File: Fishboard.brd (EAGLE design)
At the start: 47.9 x 61 mm, 23 parts, among them J3 B1, J4 B2, J5 B3, J7 B4, Q1 FQP30N06L, Q2 FQP30N06L, Q3 FQP30N06L

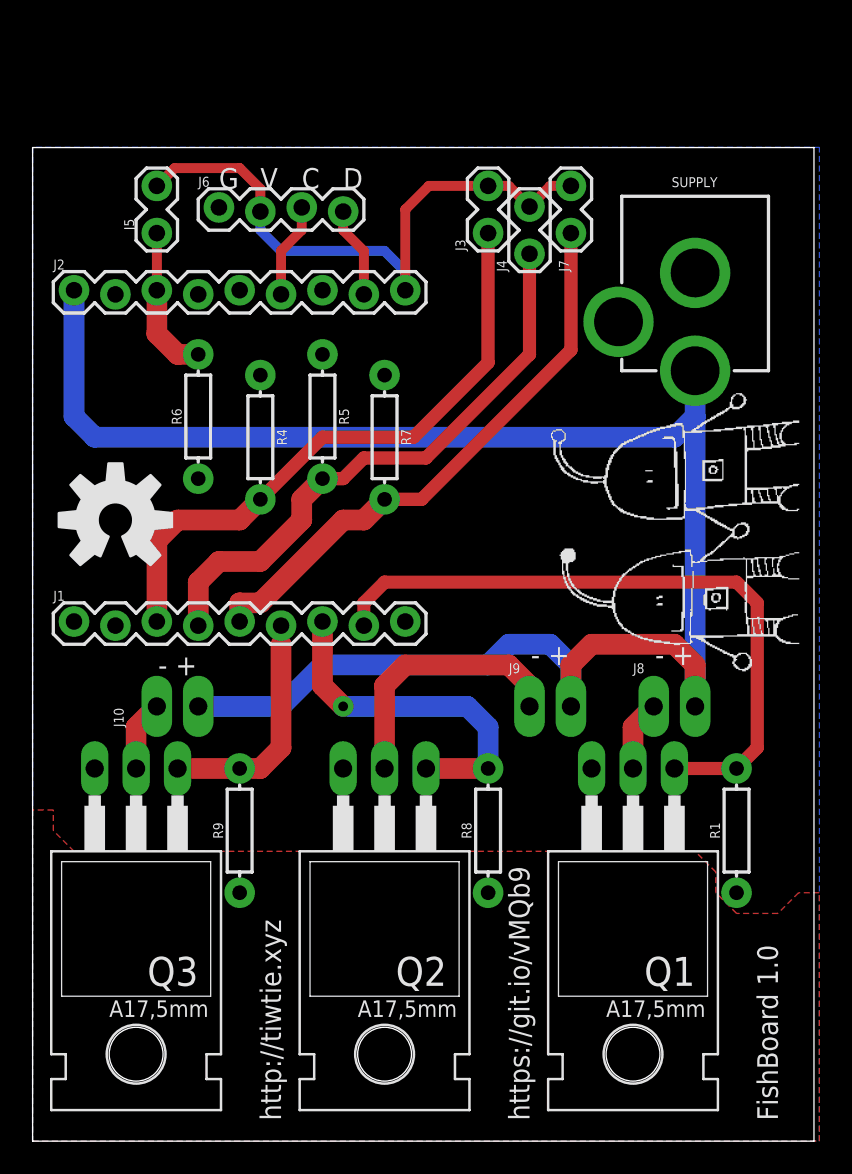
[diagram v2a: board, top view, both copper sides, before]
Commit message: Replaced TIP120 part with custom part so that we can correctly route it.
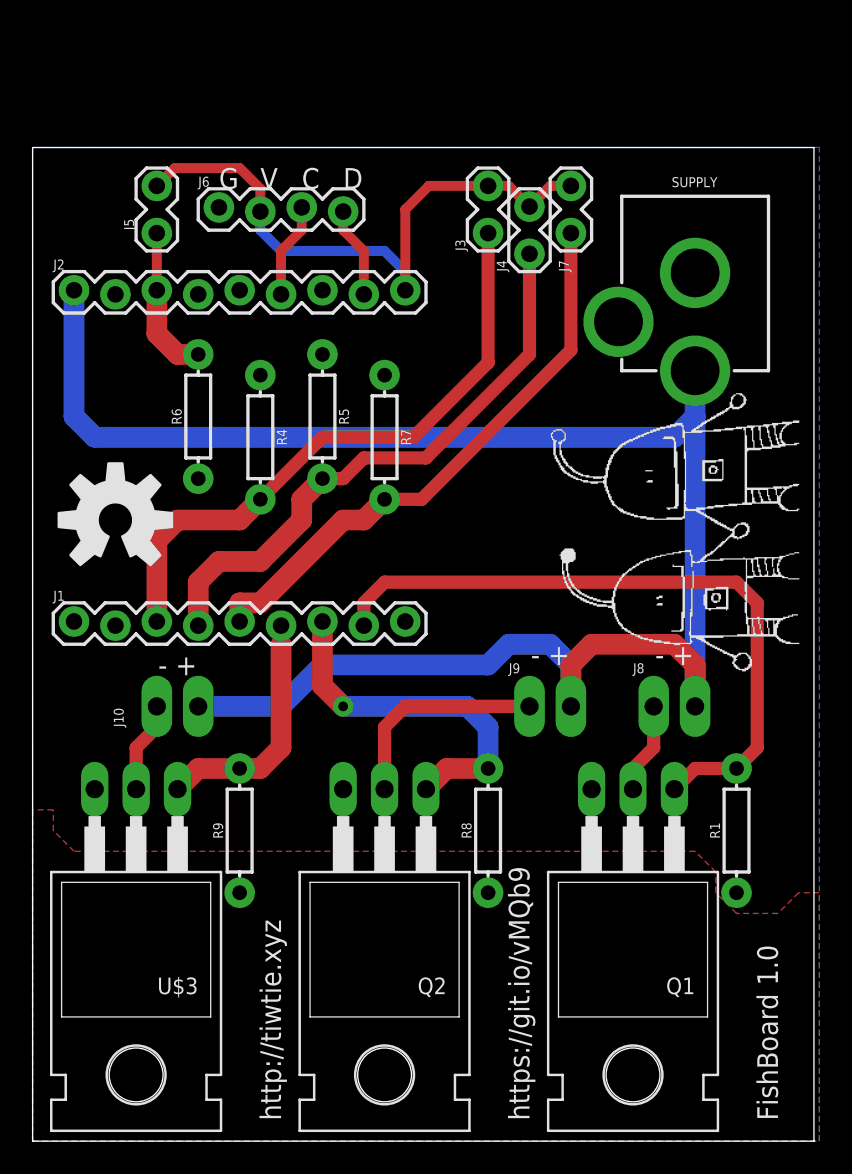
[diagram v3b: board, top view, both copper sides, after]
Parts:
- removed Q3: FQP30N06L, transistor-power:TO220AH
- added U$3: FQP30N06L, fishlib:TO220
- Q1, Q2: device transistor-power:TO220AH -> fishlib:TO220
- moved Q1 1.27 mm to (36.8, 15.2)
- moved Q2 1.27 mm to (21.6, 15.2)
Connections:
- removed net N$5: J9.1, Q2.C
- removed net N$6: J10.1, Q3.C
- new net N$2: J8.1, Q1.D
- new net N$4: J10.1, U$3.D
- net DEV1_EN: now also Q1.G; no longer Q1.B
- net DEV2_EN: now also Q2.G; no longer Q2.B
- net DEV3_EN: now also U$3.G; no longer Q3.B
- net GND: now also Q1.S, Q2.S, U$3.S; no longer Q1.E, Q2.E, Q3.E
- net N$1: now also J9.1, Q2.D; no longer J8.1, Q1.C
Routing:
- net N$5: track 16.3 -> 0.00 mm
- net N$1: track 4.34 -> 13.2 mm
- net N$2: track 0.00 -> 5.61 mm
- net N$4: track 0.00 -> 5.61 mm
- net N$6: track 4.34 -> 0.00 mm
- net DEV3_EN: track 14.4 -> 14.9 mm
- net DEV2_EN: track 21.5 -> 22.0 mm
- net DEV1_EN: track 41.1 -> 41.6 mm
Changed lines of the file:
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@@
 <element name="J1" library="SparkFun-Connectors" package="1X09_LOCK" value="" x="2.54" y="31.75"/>
 <element name="J2" library="SparkFun-Connectors" package="1X09_LOCK" value="" x="2.54" y="52.07"/>
-<element name="Q1" library="transistor-power" package="TO220AH" value="FQP30N06L" x="36.83" y="16.51" smashed="yes" rot="R180">
-<attribute name="NAME" x="40.64" y="11.303" size="1.778" layer="25" ratio="10" rot="R180"/>
-<attribute name="VALUE" x="40.767" y="13.97" size="1.016" layer="27" font="vector" ratio="10" rot="R180"/>
-</element>
-<element name="Q2" library="transistor-power" package="TO220AH" value="FQP30N06L" x="21.59" y="16.51" smashed="yes" rot="R180">
-<attribute name="NAME" x="25.4" y="11.303" size="1.778" layer="25" ratio="10" rot="R180"/>
-<attribute name="VALUE" x="25.527" y="13.97" size="1.016" layer="27" font="vector" ratio="10" rot="R180"/>
-</element>
-<element name="Q3" library="transistor-power" package="TO220AH" value="FQP30N06L" x="6.35" y="16.51" smashed="yes" rot="R180">
-<attribute name="NAME" x="10.16" y="11.303" size="1.778" layer="25" ratio="10" rot="R180"/>
-<attribute name="VALUE" x="10.287" y="13.97" size="1.016" layer="27" font="vector" ratio="10" rot="R180"/>
-</element>
 <element name="SUPPLY" library="SparkFun-Connectors" package="POWER_JACK_PTH" value="POWER_JACK" x="40.64" y="60.96" rot="R180">
 <attribute name="PROD_ID" value="CONN-08197" x="40.64" y="60.96" size="1.778" layer="27" rot="R180" display="off"/>
@@
 <attribute name="VALUE" x="12.446" y="20.32" size="0.6096" layer="27" font="vector" ratio="20" rot="R90" align="top-center"/>
 </element>
+<element name="Q1" library="fishlib" package="TO220" value="FQP30N06L" x="36.83" y="15.24" rot="R180"/>
+<element name="Q2" library="fishlib" package="TO220" value="FQP30N06L" x="21.59" y="15.24" rot="R180"/>
+<element name="U$3" library="fishlib" package="TO220" value="FQP30N06L" x="6.35" y="15.24" rot="R180"/>
 </elements>
 <signals>
@@
 <contactref element="SUPPLY" pad="GND"/>
 <contactref element="SUPPLY" pad="GNDBREAK"/>
-<contactref element="Q2" pad="E"/>
-<contactref element="Q1" pad="E"/>
-<contactref element="Q3" pad="E"/>
 <contactref element="J2" pad="2"/>
 <contactref element="J1" pad="9"/>
@@
 <contactref element="R8" pad="P$1"/>
 <contactref element="R9" pad="P$1"/>
+<contactref element="Q1" pad="S"/>
+<contactref element="Q2" pad="S"/>
+<contactref element="U$3" pad="S"/>
 </signal>
 <signal name="VCC12">
@@
 <wire x1="33.02" y1="29.21" x2="33.02" y2="26.67" width="1.27" layer="16"/>
 </signal>
-<signal name="N$1">
-<contactref element="Q1" pad="C"/>
-<contactref element="J8" pad="1"/>
-<wire x1="38.1" y1="26.67" x2="36.83" y2="25.4" width="1.27" layer="1"/>
-<wire x1="36.83" y1="25.4" x2="36.83" y2="22.86" width="1.27" layer="1"/>
-</signal>
 <signal name="DEV1_EN">
 <contactref element="J1" pad="8"/>
@@
 <wire x1="43.18" y1="34.29" x2="44.45" y2="33.02" width="0.8128" layer="1"/>
 <contactref element="R1" pad="P$2"/>
-<contactref element="Q1" pad="B"/>
+<contactref element="Q1" pad="G"/>
 <wire x1="44.45" y1="33.02" x2="44.45" y2="24.13" width="0.8128" layer="1"/>
 <wire x1="44.45" y1="24.13" x2="43.18" y2="22.86" width="0.8128" layer="1"/>
-<wire x1="39.37" y1="22.86" x2="43.18" y2="22.86" width="0.8128" layer="1"/>
+<wire x1="39.37" y1="21.59" x2="40.64" y2="22.86" width="0.8128" layer="1"/>
+<wire x1="40.64" y1="22.86" x2="43.18" y2="22.86" width="0.8128" layer="1"/>
 </signal>
 <signal name="DEV2_EN">
@@
 <wire x1="17.78" y1="31.877" x2="17.78" y2="27.94" width="1.27" layer="1"/>
 <contactref element="R8" pad="P$2"/>
-<contactref element="Q2" pad="B"/>
-<wire x1="24.13" y1="22.86" x2="27.94" y2="22.86" width="1.27" layer="1"/>
 <wire x1="17.78" y1="27.94" x2="19.05" y2="26.67" width="1.27" layer="1"/>
 <via x="19.05" y="26.67" extent="1-16" drill="0.6" diameter="1.27"/>
@@
 <wire x1="26.67" y1="26.67" x2="27.94" y2="25.4" width="1.27" layer="16"/>
 <wire x1="27.94" y1="25.4" x2="27.94" y2="22.86" width="1.27" layer="16"/>
+<contactref element="Q2" pad="G"/>
+<wire x1="24.13" y1="21.59" x2="25.4" y2="22.86" width="1.27" layer="1"/>
+<wire x1="25.4" y1="22.86" x2="27.94" y2="22.86" width="1.27" layer="1"/>
 </signal>
 <signal name="DEV3_EN">
@@
 <wire x1="15.24" y1="31.623" x2="15.24" y2="30.48" width="0.6096" layer="1"/>
 <contactref element="R9" pad="P$2"/>
-<contactref element="Q3" pad="B"/>
 <wire x1="15.24" y1="30.48" x2="15.24" y2="24.13" width="1.27" layer="1"/>
 <wire x1="15.24" y1="24.13" x2="13.97" y2="22.86" width="1.27" layer="1"/>
 <wire x1="13.97" y1="22.86" x2="12.7" y2="22.86" width="1.27" layer="1"/>
-<wire x1="8.89" y1="22.86" x2="12.7" y2="22.86" width="1.27" layer="1"/>
+<contactref element="U$3" pad="G"/>
+<wire x1="8.89" y1="21.59" x2="10.16" y2="22.86" width="1.27" layer="1"/>
+<wire x1="10.16" y1="22.86" x2="12.7" y2="22.86" width="1.27" layer="1"/>
 </signal>
 <signal name="D9">
@@
 <wire x1="27.94" y1="47.75905" x2="27.94" y2="55.7022" width="0.8128" layer="1"/>
 </signal>
-<signal name="N$6">
-<contactref element="Q3" pad="C"/>
-<contactref element="J10" pad="1"/>
-<wire x1="7.62" y1="26.67" x2="6.35" y2="25.4" width="1.27" layer="1"/>
-<wire x1="6.35" y1="25.4" x2="6.35" y2="22.86" width="1.27" layer="1"/>
-</signal>
 <signal name="DATA">
 <contactref element="J6" pad="4"/>
@@
 <wire x1="16.51" y1="55.88" x2="15.24" y2="54.61" width="0.6096" layer="1"/>
 <wire x1="15.24" y1="54.61" x2="15.24" y2="51.943" width="0.6096" layer="1"/>
-</signal>
-<signal name="N$5">
-<contactref element="Q2" pad="C"/>
-<contactref element="J9" pad="1"/>
-<wire x1="21.59" y1="22.86" x2="21.59" y2="27.94" width="1.27" layer="1"/>
-<wire x1="21.59" y1="27.94" x2="22.86" y2="29.21" width="1.27" layer="1"/>
-<wire x1="22.86" y1="29.21" x2="29.21" y2="29.21" width="1.27" layer="1"/>
-<wire x1="29.21" y1="29.21" x2="30.48" y2="27.94" width="1.27" layer="1"/>
-<wire x1="30.48" y1="27.94" x2="30.48" y2="26.67" width="1.27" layer="1"/>
 </signal>
 <signal name="N$7">
@@
 </polygon>
 </signal>
+<signal name="N$2">
+<contactref element="Q1" pad="D"/>
+<contactref element="J8" pad="1"/>
+<wire x1="38.1" y1="26.67" x2="38.1" y2="24.13" width="0.8128" layer="1"/>
+<wire x1="38.1" y1="24.13" x2="36.83" y2="22.86" width="0.8128" layer="1"/>
+<wire x1="36.83" y1="22.86" x2="36.83" y2="21.59" width="0.8128" layer="1"/>
+</signal>
+<signal name="N$1">
+<contactref element="J9" pad="1"/>
+<contactref element="Q2" pad="D"/>
+<wire x1="30.48" y1="26.67" x2="22.86" y2="26.67" width="0.8128" layer="1"/>
+<wire x1="22.86" y1="26.67" x2="21.59" y2="25.4" width="0.8128" layer="1"/>
+<wire x1="21.59" y1="25.4" x2="21.59" y2="21.59" width="0.8128" layer="1"/>
+</signal>
+<signal name="N$4">
+<contactref element="U$3" pad="D"/>
+<contactref element="J10" pad="1"/>
+<wire x1="7.62" y1="26.67" x2="7.62" y2="25.4" width="0.8128" layer="1"/>
+<wire x1="7.62" y1="25.4" x2="6.35" y2="24.13" width="0.8128" layer="1"/>
+<wire x1="6.35" y1="24.13" x2="6.35" y2="21.59" width="0.8128" layer="1"/>
+</signal>
 </signals>

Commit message: Moved Open Source Hardware logo to bottom of board. Added flyback diodes.
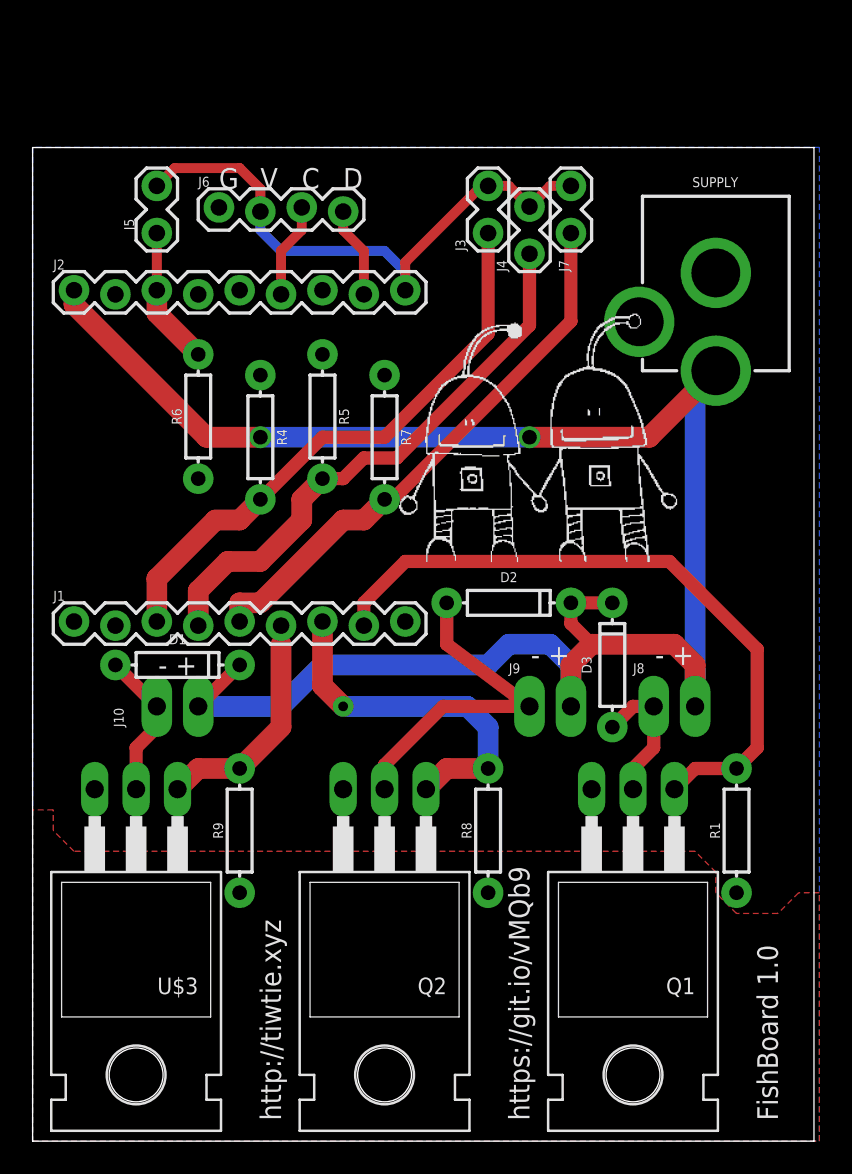
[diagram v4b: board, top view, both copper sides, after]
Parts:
- added D1, D2, D3: 200mA/100V/1V, SparkFun-DiscreteSemi:DIODE-1N4148-KIT
- moved U$1 26.5 mm to (21.6, 35.6), turned to 0 degrees
- moved SUPPLY 1.27 mm to (41.9, 61.0)
- flipped U$2 to the bottom
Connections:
- net N$1: now also D2.A
- net N$2: now also D3.A
- net N$4: now also D1.A
- net VCC12: now also D1.C, D2.C, D3.C
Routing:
- net VCC12: track 110.0 -> 118.1 mm, vias 0 -> 2
- net N$1: track 13.2 -> 20.8 mm
- net N$4: track 5.61 -> 9.20 mm
- net N$2: track 5.61 -> 8.67 mm
- net D11: track 37.7 -> 35.3 mm
- net VCC3V3: track 37.7 -> 35.8 mm
- net D10: track 35.7 -> 34.3 mm
- net D9: track 35.1 -> 34.0 mm
- net DEV3_EN: track 14.9 -> 14.2 mm
- net D5: track 9.24 -> 8.49 mm
- net DEV1_EN: track 41.6 -> 41.0 mm

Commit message: Changed the board size and rerouted everything to make the board fit the case I selected
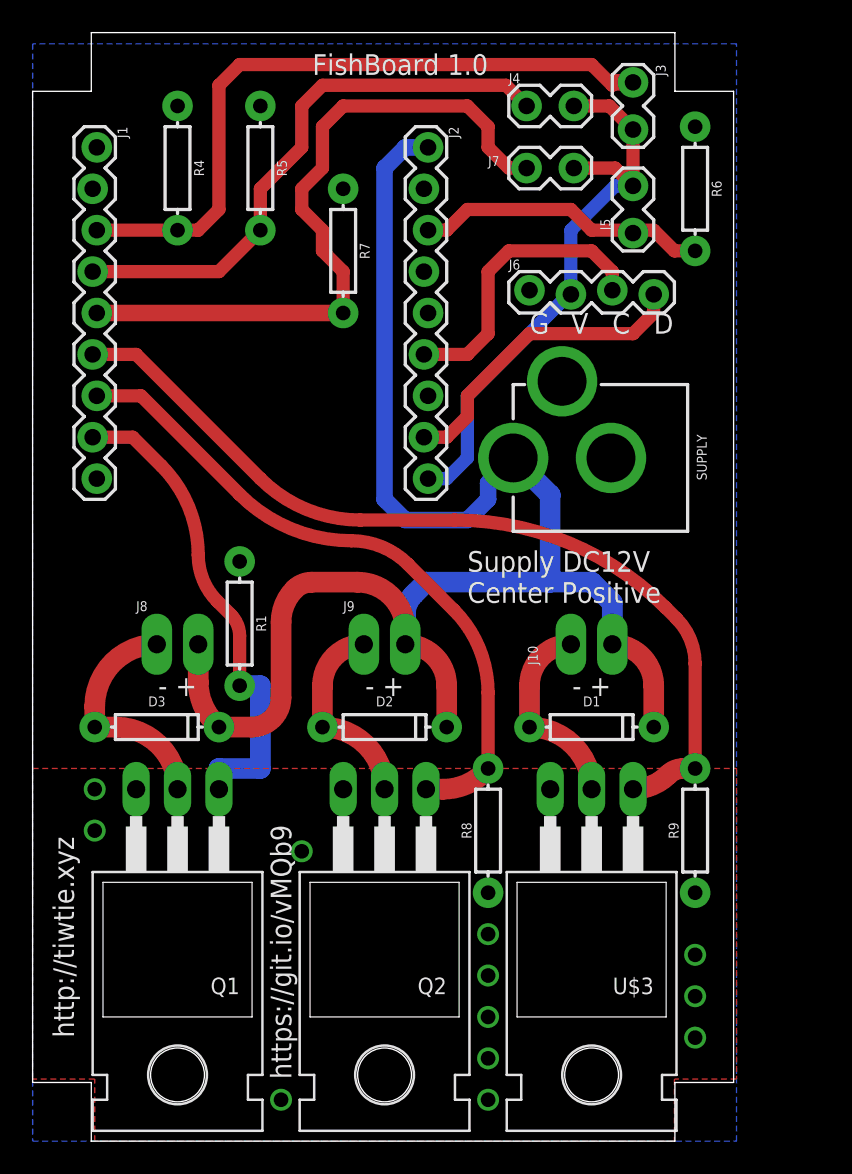
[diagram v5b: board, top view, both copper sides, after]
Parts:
- moved R6 33.5 mm to (40.6, 58.4), turned to 270 degrees
- moved R1 33.0 mm to (12.7, 31.8), turned to 270 degrees
- moved J8 30.7 mm to (7.62, 30.5)
- moved J1 29.2 mm to (3.81, 61.0), turned to 270 degrees
- moved J5 29.2 mm to (36.8, 58.4)
- moved D3 28.2 mm to (7.62, 25.4), turned to 0 degrees
- moved R9 27.9 mm to (40.6, 19.1)
- moved Q1 27.9 mm to (8.89, 15.2)
- moved U$3 27.9 mm to (34.3, 15.2)
- moved J10 25.7 mm to (33.0, 30.5)
- moved D1 25.7 mm to (34.3, 25.4)
- moved J2 23.3 mm to (24.1, 61.0), turned to 270 degrees
- moved U$2 23.2 mm to (27.9, 34.3)
- moved J6 19.7 mm to (30.5, 52.1)
- moved SUPPLY 19.1 mm to (43.2, 41.9), turned to 90 degrees
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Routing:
- net DEV3_EN: track 14.2 -> 54.3 mm
- net VCC12: track 118.1 -> 99.4 mm, vias 2 -> 0
- net DEV2_EN: track 22.0 -> 40.7 mm, vias 1 -> 0
- net DATA: track 5.61 -> 19.1 mm
- net CLOCK: track 5.86 -> 18.1 mm
- net DEV1_EN: track 41.0 -> 29.7 mm
- net D5: track 8.49 -> 18.1 mm
- net D9: track 34.0 -> 43.5 mm
- net N$1: track 20.8 -> 11.5 mm
- net D11: track 35.3 -> 42.3 mm
- net N$2: track 8.67 -> 13.3 mm
- net N$4: track 9.20 -> 11.5 mm
- net D10: track 34.3 -> 34.9 mm
- added copper zone on layer 1, net GND
- removed copper zone on layer 1, net N$7
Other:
- board size 47.9 x 61 mm -> 43 x 68 mm
- board text added: "Supply DC12V Center Positive"
